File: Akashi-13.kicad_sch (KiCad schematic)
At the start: 39 parts, among them J1 Conn_02x35_Odd_Even, J2 Conn_02x35_Odd_Even, J3 J0011D01BNL, U1 LAN9220-ABZJ, U2 93AA46AT-IOT, X1 DFA-S15

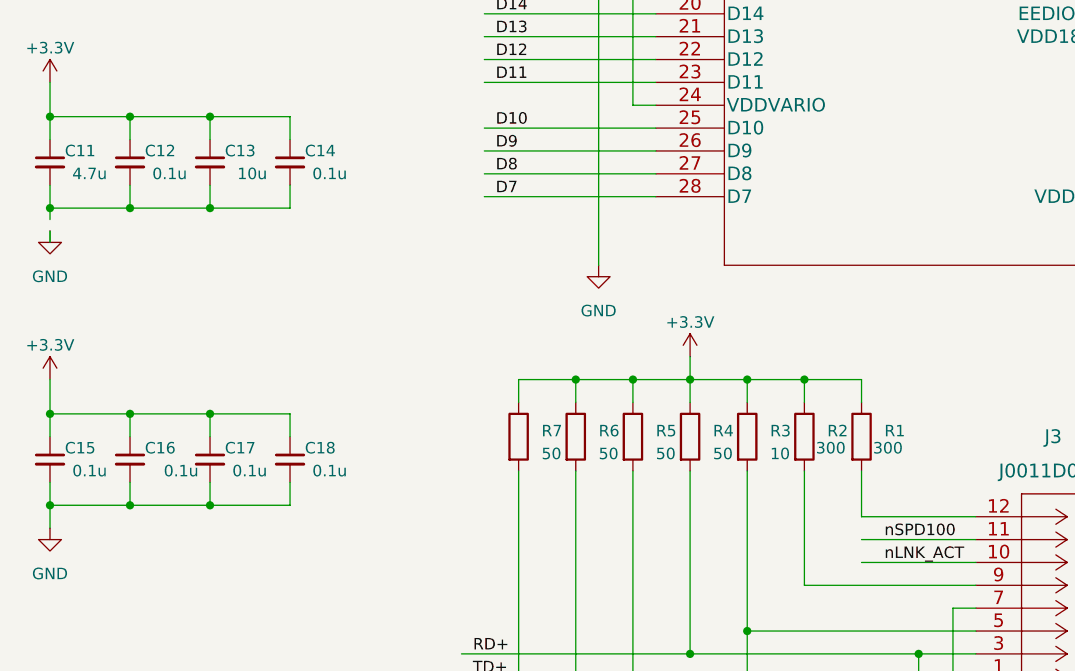
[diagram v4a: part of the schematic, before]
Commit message: All bypass chapacitor of LAN9220 and XTAL are placed.
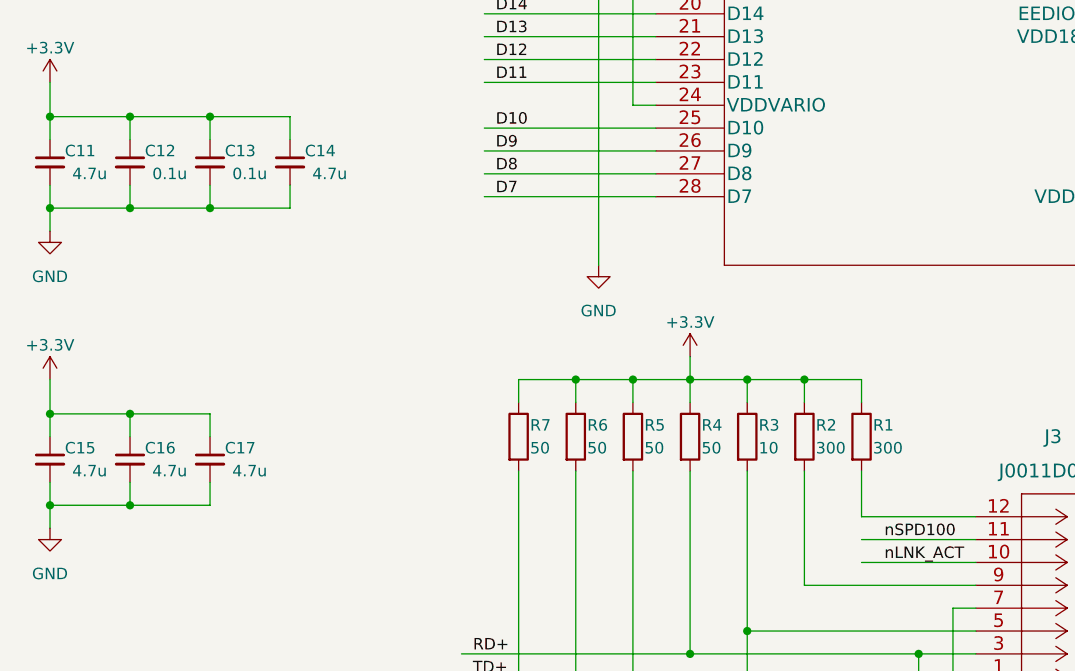
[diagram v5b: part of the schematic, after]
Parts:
- removed C18: 0.1u, Capacitor_SMD:C_0603_1608Metric_Pad1.08x0.95mm_HandSolder, symbol Device:C_Small
- C13: value 10u -> 0.1u
- C14, C15, C16, C17: value 0.1u -> 4.7u
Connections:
- net GND: now also C11.2, C12.2, C13.2, C14.2
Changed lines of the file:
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@@
   (junction (at 252.73 149.86) (diameter 0) (color 0 0 0 0)
   )
-  (junction (at 38.1 140.97) (diameter 0) (color 0 0 0 0)
-  )
   (junction (at 85.09 27.94) (diameter 0) (color 0 0 0 0)
   )
@@
   (junction (at 38.1 97.79) (diameter 0) (color 0 0 0 0)
   )
-  (junction (at 38.1 130.81) (diameter 0) (color 0 0 0 0)
-  )
   (junction (at 252.73 147.32) (diameter 0) (color 0 0 0 0)
   )
@@
     (stroke (width 0) (type default))
   )
-  (wire (pts (xy 46.99 130.81) (xy 46.99 133.35))
-    (stroke (width 0) (type default))
-  )
   (wire (pts (xy 212.09 90.17) (xy 214.63 90.17))
     (stroke (width 0) (type default))
@@
     (stroke (width 0) (type default))
   )
-  (wire (pts (xy 20.32 110.49) (xy 20.32 111.76))
-    (stroke (width 0) (type default))
-  )
   (wire (pts (xy 231.14 138.43) (xy 231.14 142.24))
     (stroke (width 0) (type default))
@@
     (stroke (width 0) (type default))
   )
-  (wire (pts (xy 46.99 138.43) (xy 46.99 140.97))
-    (stroke (width 0) (type default))
-  )
   (wire (pts (xy 113.03 160.02) (xy 113.03 175.26))
     (stroke (width 0) (type default))
@@
     (stroke (width 0) (type default))
   )
-  (wire (pts (xy 38.1 140.97) (xy 46.99 140.97))
-    (stroke (width 0) (type default))
-  )
   (wire (pts (xy 66.04 170.18) (xy 72.39 170.18))
     (stroke (width 0) (type default))
@@
     (stroke (width 0) (type default))
   )
-  (wire (pts (xy 20.32 107.95) (xy 20.32 109.22))
+  (wire (pts (xy 20.32 107.95) (xy 20.32 110.49))
     (stroke (width 0) (type default))
   )
@@
     (stroke (width 0) (type default))
   )
-  (wire (pts (xy 38.1 130.81) (xy 46.99 130.81))
-    (stroke (width 0) (type default))
-  )
   (wire (pts (xy 267.97 52.07) (xy 267.97 67.31))
     (stroke (width 0) (type default))
@@
     )
   )
-  (symbol (lib_id "Device:C_Small") (at 46.99 135.89 0) (mirror y) (unit 1)
-    (in_bom yes) (on_board yes) (dnp no)
-    (property "Reference" "C18" (at 52.07 134.62 0)
-      (effects (font (size 1.27 1.27)) (justify left))
-    )
-    (property "Value" "0.1u" (at 53.34 137.16 0)
-      (effects (font (size 1.27 1.27)) (justify left))
-    )
-    (property "Footprint" "Capacitor_SMD:C_0603_1608Metric_Pad1.08x0.95mm_HandSolder" (at 46.99 135.89 0)
-      (effects (font (size 1.27 1.27)) hide)
-    )
-    (property "Datasheet" "~" (at 46.99 135.89 0)
-      (effects (font (size 1.27 1.27)) hide)
-    )
-    (pin "1")
-    (pin "2")
-    (instances
-      (project "Akashi-13"
-        (path "/033652e2-f6e3-4f6d-863c-7fc278170639"
-          (reference "C18") (unit 1)
-        )
-      )
-    )
-  )
   (symbol (lib_id "Device:R") (at 78.74 133.35 0) (unit 1)
-    (in_bom yes) (on_board yes) (dnp no) (fields_autoplaced)
-    (property "Reference" "R6" (at 81.28 132.715 0)
+    (in_bom yes) (on_board yes) (dnp no)
+    (property "Reference" "R6" (at 80.01 132.08 0)
       (effects (font (size 1.27 1.27)) (justify left))
     )
-    (property "Value" "50" (at 81.28 135.255 0)
+    (property "Value" "50" (at 80.01 134.62 0)
       (effects (font (size 1.27 1.27)) (justify left))
     )
@@
   )
   (symbol (lib_id "Device:R") (at 91.44 133.35 0) (unit 1)
-    (in_bom yes) (on_board yes) (dnp no) (fields_autoplaced)
-    (property "Reference" "R4" (at 93.98 132.715 0)
+    (in_bom yes) (on_board yes) (dnp no)
+    (property "Reference" "R4" (at 92.71 132.08 0)
       (effects (font (size 1.27 1.27)) (justify left))
     )
-    (property "Value" "50" (at 93.98 135.255 0)
+    (property "Value" "50" (at 92.71 134.62 0)
       (effects (font (size 1.27 1.27)) (justify left))
     )
@@
       (effects (font (size 1.27 1.27)) (justify left))
     )
-    (property "Value" "0.1u" (at 26.67 137.16 0)
+    (property "Value" "4.7u" (at 26.67 137.16 0)
       (effects (font (size 1.27 1.27)) (justify left))
     )
@@
       (effects (font (size 1.27 1.27)) (justify left))
     )
-    (property "Value" "10u" (at 44.45 104.14 0)
+    (property "Value" "0.1u" (at 44.45 104.14 0)
       (effects (font (size 1.27 1.27)) (justify left))
     )
@@
   )
   (symbol (lib_id "Device:R") (at 85.09 133.35 0) (unit 1)
-    (in_bom yes) (on_board yes) (dnp no) (fields_autoplaced)
-    (property "Reference" "R5" (at 87.63 132.715 0)
+    (in_bom yes) (on_board yes) (dnp no)
+    (property "Reference" "R5" (at 86.36 132.08 0)
       (effects (font (size 1.27 1.27)) (justify left))
     )
-    (property "Value" "50" (at 87.63 135.255 0)
+    (property "Value" "50" (at 86.36 134.62 0)
       (effects (font (size 1.27 1.27)) (justify left))
     )
@@
       (effects (font (size 1.27 1.27)) (justify left))
     )
-    (property "Value" "0.1u" (at 44.45 137.16 0)
+    (property "Value" "4.7u" (at 44.45 137.16 0)
       (effects (font (size 1.27 1.27)) (justify left))
     )
@@
   )
   (symbol (lib_id "Device:R") (at 72.39 133.35 0) (unit 1)
-    (in_bom yes) (on_board yes) (dnp no) (fields_autoplaced)
-    (property "Reference" "R7" (at 74.93 132.715 0)
+    (in_bom yes) (on_board yes) (dnp no)
+    (property "Reference" "R7" (at 73.66 132.08 0)
       (effects (font (size 1.27 1.27)) (justify left))
     )
-    (property "Value" "50" (at 74.93 135.255 0)
+    (property "Value" "50" (at 73.66 134.62 0)
       (effects (font (size 1.27 1.27)) (justify left))
     )
@@
       (effects (font (size 1.27 1.27)) (justify left))
     )
-    (property "Value" "0.1u" (at 53.34 104.14 0)
+    (property "Value" "4.7u" (at 53.34 104.14 0)
       (effects (font (size 1.27 1.27)) (justify left))
     )
@@
       (effects (font (size 1.27 1.27)) (justify left))
     )
-    (property "Value" "0.1u" (at 36.83 137.16 0)
+    (property "Value" "4.7u" (at 35.56 137.16 0)
       (effects (font (size 1.27 1.27)) (justify left))
     )
@@
   (symbol (lib_id "Device:R") (at 110.49 133.35 0) (unit 1)
     (in_bom yes) (on_board yes) (dnp no)
-    (property "Reference" "R1" (at 113.03 132.715 0)
+    (property "Reference" "R1" (at 111.76 132.08 0)
       (effects (font (size 1.27 1.27)) (justify left))
     )
@@
   )
   (symbol (lib_id "Device:R") (at 97.79 133.35 0) (unit 1)
-    (in_bom yes) (on_board yes) (dnp no) (fields_autoplaced)
-    (property "Reference" "R3" (at 100.33 132.715 0)
+    (in_bom yes) (on_board yes) (dnp no)
+    (property "Reference" "R3" (at 99.06 132.08 0)
       (effects (font (size 1.27 1.27)) (justify left))
     )
-    (property "Value" "10" (at 100.33 135.255 0)
+    (property "Value" "10" (at 99.06 134.62 0)
       (effects (font (size 1.27 1.27)) (justify left))
     )
@@
   (symbol (lib_id "Device:R") (at 104.14 133.35 0) (unit 1)
     (in_bom yes) (on_board yes) (dnp no)
-    (property "Reference" "R2" (at 106.68 132.715 0)
+    (property "Reference" "R2" (at 105.41 132.08 0)
       (effects (font (size 1.27 1.27)) (justify left))
     )

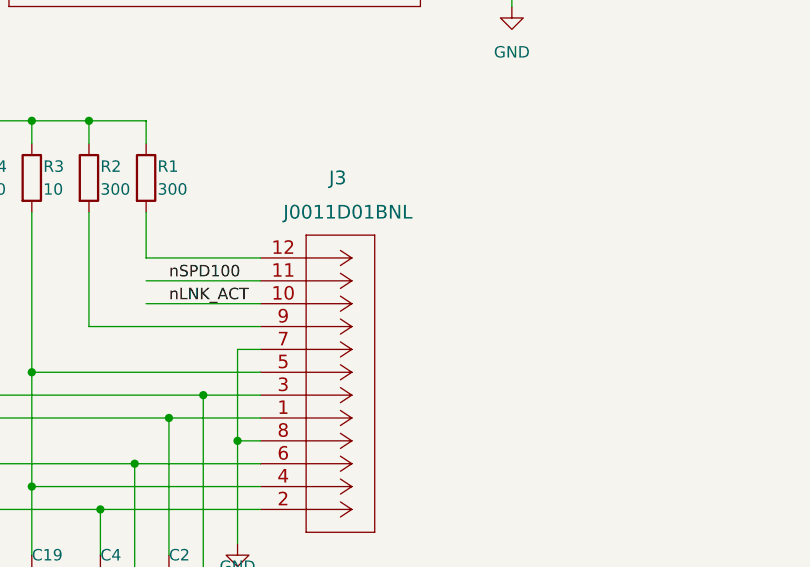
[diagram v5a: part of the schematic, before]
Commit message: Add comment on the board.
JB1
LEDs
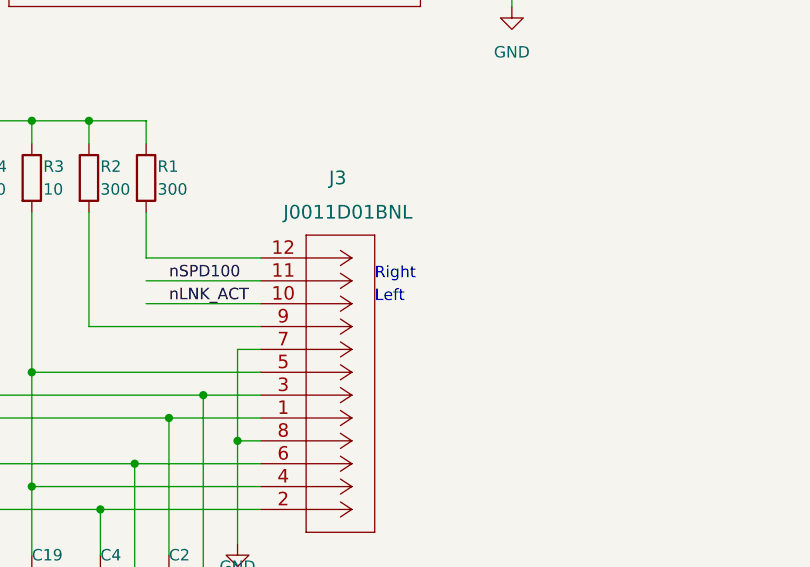
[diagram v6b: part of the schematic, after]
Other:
- note added: "Left"
- note added: "Right"
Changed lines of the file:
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@@
     (stroke (width 0) (type default))
+  )
+  (text "Right" (at 135.89 144.78 0)
+    (effects (font (size 1.27 1.27)) (justify left bottom))
   )
   (text "The WAKEUP and IRQ signal have to be pulled up by MCU."
@@
     (effects (font (size 1.27 1.27)) (justify left bottom))
   )
+  (text "Left" (at 135.89 147.32 0)
+    (effects (font (size 1.27 1.27)) (justify left bottom))
+  )

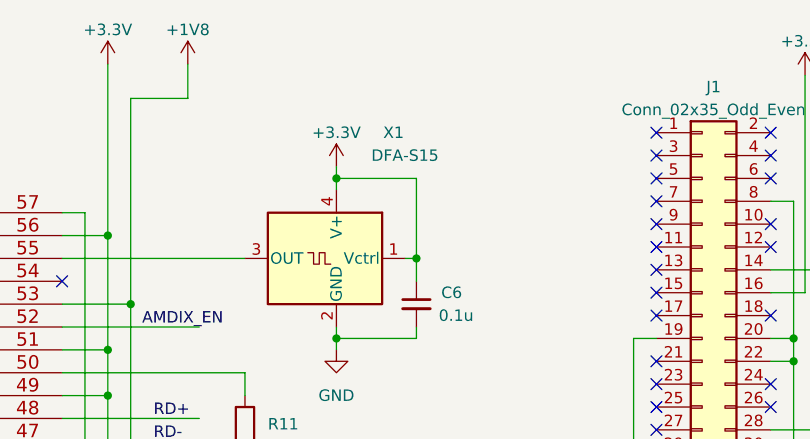
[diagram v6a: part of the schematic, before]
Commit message: Add vias to the exposed pad of U1.
Also following FusionPCB rules.
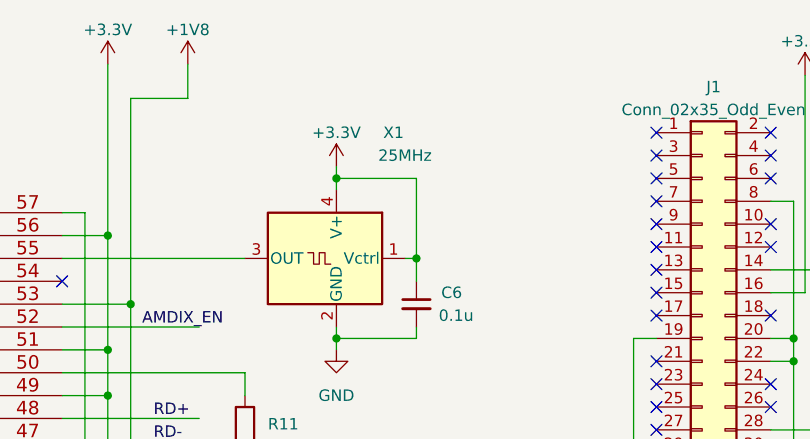
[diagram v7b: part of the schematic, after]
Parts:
- X1: value DFA-S15 -> 25MHz
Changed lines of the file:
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@@
       (effects (font (size 1.27 1.27)))
     )
-    (property "Value" "DFA-S15" (at 186.69 31.75 0)
+    (property "Value" "25MHz" (at 186.69 31.75 0)
       (effects (font (size 1.27 1.27)))
     )
